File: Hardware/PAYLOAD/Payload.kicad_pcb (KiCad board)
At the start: 4 copper layers, 85 x 85 mm, 59 parts, among them J201 Conn_ARM_JTAG_SWD_10, J401 USB_C_Receptacle_PowerOnly_6P, J601 Conn_02x20_Odd_Even, M1201 MountingHole_Pad, M1202 MountingHole_Pad, M1203 MountingHole_Pad, M1204 MountingHole_Pad, U201 STM32L431RCT, U202 HZ0805E601R-10, U401 AP7361C-33Y5-13

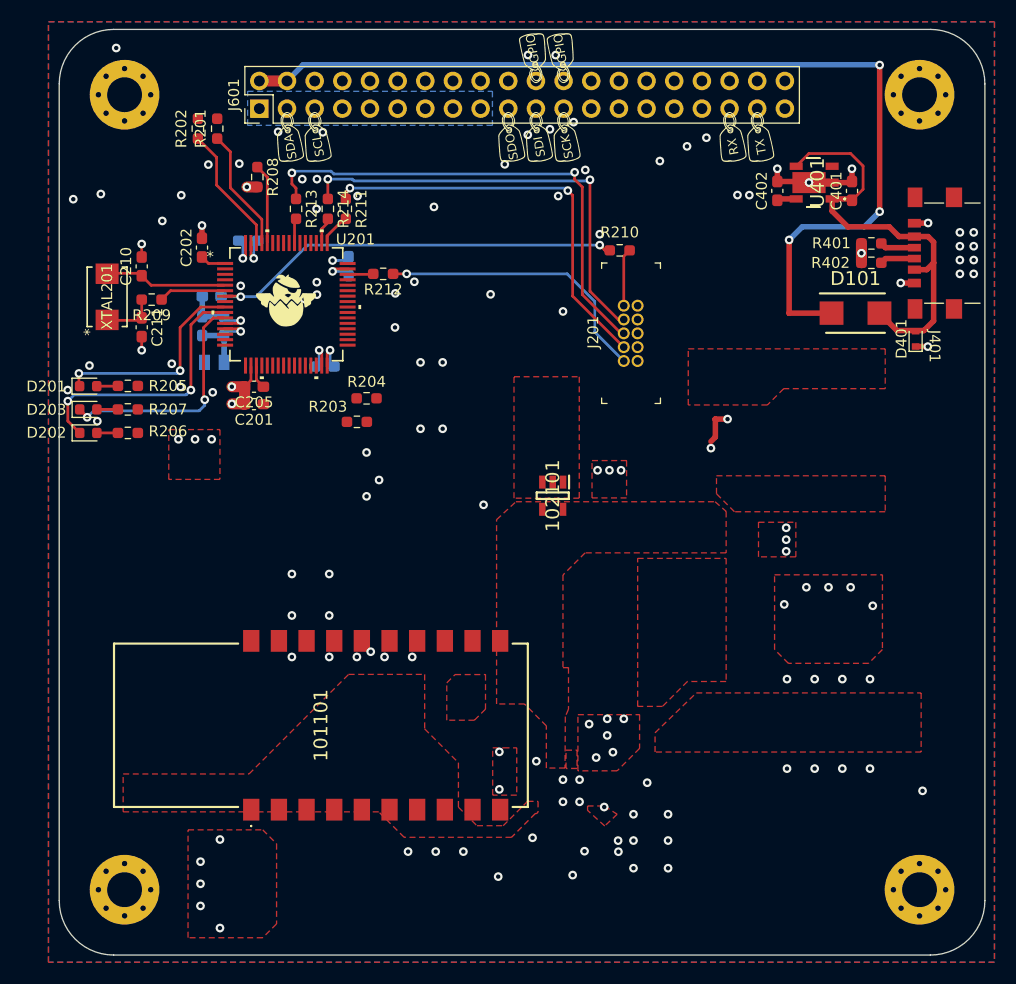
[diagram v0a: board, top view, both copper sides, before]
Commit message: Updated to KiCAD 7.0
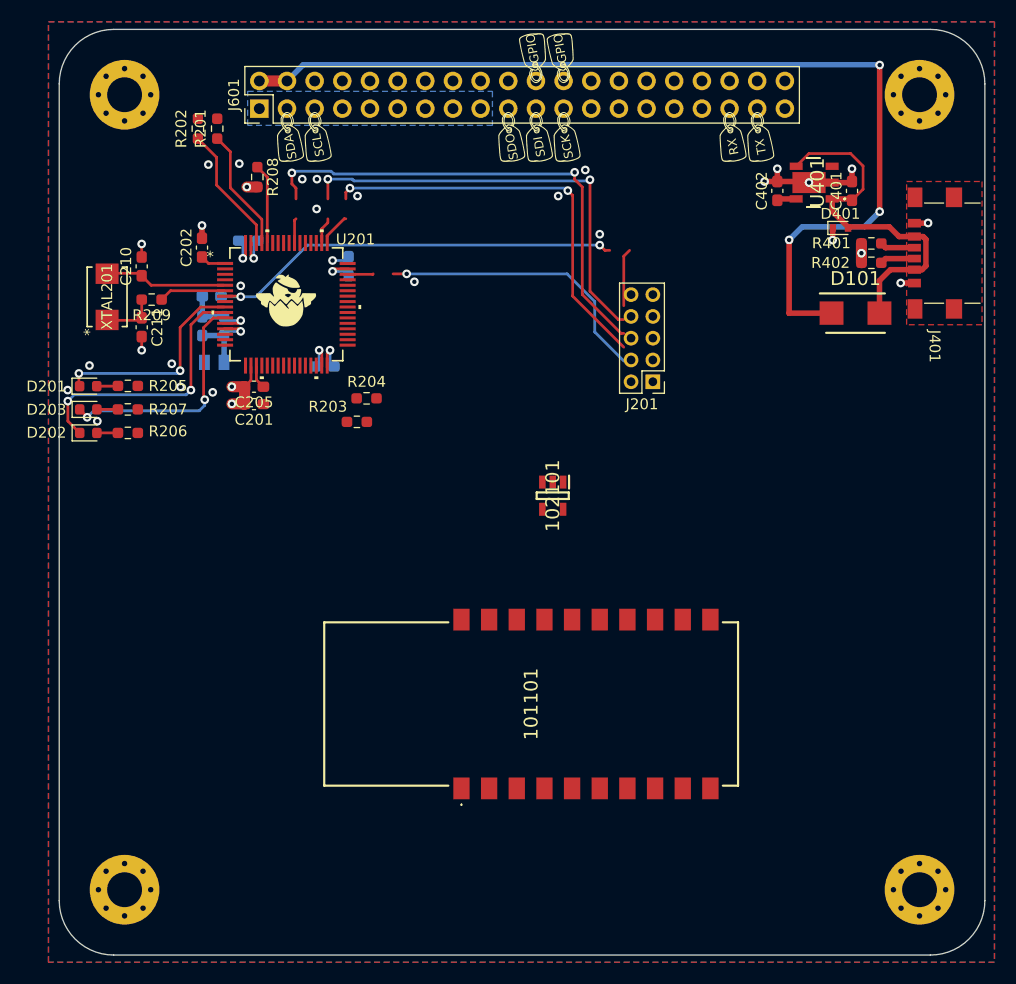
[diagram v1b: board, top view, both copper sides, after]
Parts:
- removed the G002 at (122.9, 115.8)
- removed R210, R211, R212, R213, R214: 22, Resistor_SMD:R_0603_1608Metric_Pad0.98x0.95mm_HandSolder
- added G***: LOGO, LOGO, B.Cu at (147.9, 124.1)
- J201: footprint digikey-footprints:PinHeader_2x5_P1.27mm_Drill.7mm -> Connector_PinHeader_2.00mm:PinHeader_2x05_P2.00mm_Vertical
- moved 101101 19.4 mm to (152.4, 122.3)
- moved D401 12.3 mm to (180.8, 78.6), turned to 0 degrees
- moved J201 2.37 mm to (163.6, 92.7), turned to 180 degrees
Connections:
- J201 pad 10: Net-(J201-Pad10) -> /STM32 MCU/NRST
- J201 pad 2: Net-(J201-Pad2) -> /STM32 MCU/JTMS
- J201 pad 4: Net-(J201-Pad4) -> /STM32 MCU/JTCK
- J201 pad 6: Net-(J201-Pad6) -> /STM32 MCU/JTDO
- J201 pad 8: Net-(J201-Pad8) -> /STM32 MCU/JTDI
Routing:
- net Net-(J201-Pad8): track 40.4 -> 0.00 mm, vias 2 -> 0
- net /STM32 MCU/JTDI: track 2.34 -> 42.7 mm, vias 0 -> 2
- net Net-(J201-Pad2): track 26.1 -> 0.00 mm, vias 1 -> 0
- net /STM32 MCU/JTCK: track 2.91 -> 29.0 mm, vias 0 -> 1
- net /USB Power/USB_VBUS: track 39.4 -> 33.6 mm
- net Net-(J201-Pad10): track 5.30 -> 0.00 mm
- net /STM32 MCU/NRST: track 39.4 -> 44.7 mm
- net GND: track 45.9 -> 43.7 mm, vias 115 -> 35
- net unconnected-(101101-Pad16): vias 1 -> 0
- net +3.3V: vias 33 -> 3
- added copper zone on F.Cu, net unconnected-(J401-PadS1)
- removed copper zone on F.Cu, net (none)
- removed copper zone on F.Cu, net GND
